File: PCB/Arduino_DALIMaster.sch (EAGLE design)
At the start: 13 parts, among them J1 22-27-2021-02, U1 ARDUINOR3-BPLACE

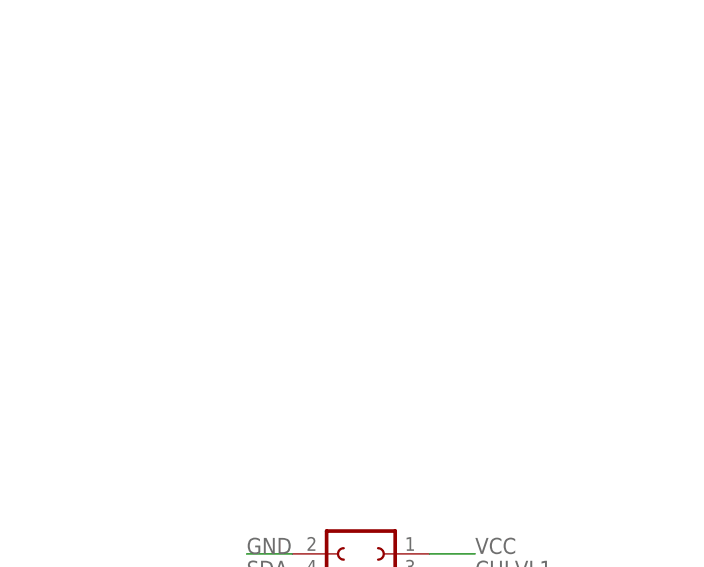
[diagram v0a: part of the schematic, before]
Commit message: SMT parts and rerouting
replaced all wired passives with 0603 SMT packages, rewired some of the
connections, reduced board size to 80x90mm
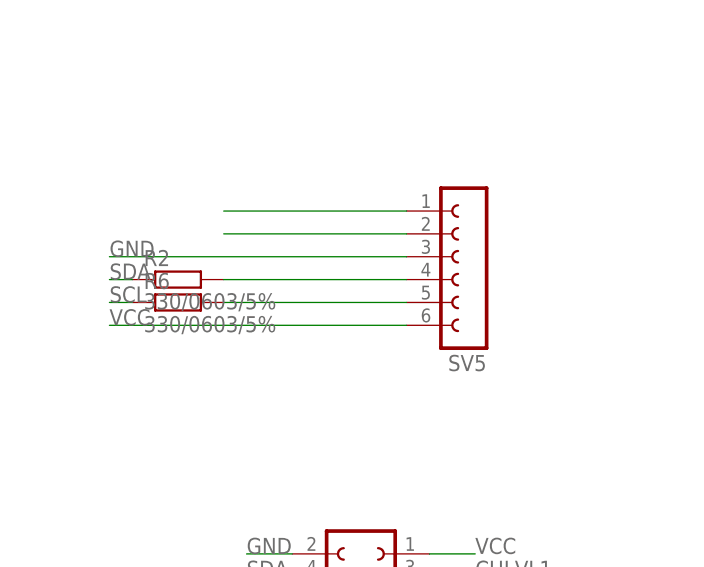
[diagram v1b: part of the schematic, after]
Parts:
- added R2, R6: 330/0603/5%, rcl:R-EU_R0603
- added SV5: (no value), con-lsta:FE06-1
- 2K7, R1, R3, R4, R5: device rcl:R-EU_0207/10 -> rcl:R-EU_R0603
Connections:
- new net N$2: SV5.1
- new net N$3: SV5.2
- new net N$5: R2.2, SV5.4
- new net N$6: R6.2, SV5.5
- net GND: now also SV5.3
- net SCL: now also R6.1
- net SDA: now also R2.1
- net VCC: now also SV5.6
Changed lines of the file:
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@@
 <grid distance="0.1" unitdist="inch" unit="inch" style="lines" multiple="1" display="no" altdistance="0.01" altunitdist="inch" altunit="inch"/>
 <layers>
-<layer number="1" name="Top" color="4" fill="1" visible="no" active="no"/>
-<layer number="16" name="Bottom" color="1" fill="1" visible="no" active="no"/>
-<layer number="17" name="Pads" color="2" fill="1" visible="no" active="no"/>
-<layer number="18" name="Vias" color="2" fill="1" visible="no" active="no"/>
-<layer number="19" name="Unrouted" color="6" fill="1" visible="no" active="no"/>
-<layer number="20" name="Dimension" color="15" fill="1" visible="no" active="no"/>
-<layer number="21" name="tPlace" color="14" fill="1" visible="no" active="no"/>
-<layer number="22" name="bPlace" color="7" fill="1" visible="no" active="no"/>
-<layer number="23" name="tOrigins" color="15" fill="1" visible="no" active="no"/>
-<layer number="24" name="bOrigins" color="15" fill="1" visible="no" active="no"/>
-<layer number="25" name="tNames" color="7" fill="1" visible="no" active="no"/>
-<layer number="26" name="bNames" color="7" fill="1" visible="no" active="no"/>
-<layer number="27" name="tValues" color="7" fill="1" visible="no" active="no"/>
-<layer number="28" name="bValues" color="7" fill="1" visible="no" active="no"/>
+<layer number="1" name="Top" color="4" fill="1" visible="yes" active="no"/>
+<layer number="16" name="Bottom" color="1" fill="1" visible="yes" active="no"/>
+<layer number="17" name="Pads" color="2" fill="1" visible="yes" active="no"/>
+<layer number="18" name="Vias" color="2" fill="1" visible="yes" active="no"/>
+<layer number="19" name="Unrouted" color="6" fill="1" visible="yes" active="no"/>
+<layer number="20" name="Dimension" color="15" fill="1" visible="yes" active="no"/>
+<layer number="21" name="tPlace" color="7" fill="1" visible="yes" active="no"/>
+<layer number="22" name="bPlace" color="7" fill="1" visible="yes" active="no"/>
+<layer number="23" name="tOrigins" color="15" fill="1" visible="yes" active="no"/>
+<layer number="24" name="bOrigins" color="15" fill="1" visible="yes" active="no"/>
+<layer number="25" name="tNames" color="7" fill="1" visible="yes" active="no"/>
+<layer number="26" name="bNames" color="7" fill="1" visible="yes" active="no"/>
+<layer number="27" name="tValues" color="7" fill="1" visible="yes" active="no"/>
+<layer number="28" name="bValues" color="7" fill="1" visible="yes" active="no"/>
 <layer number="29" name="tStop" color="7" fill="3" visible="no" active="no"/>
 <layer number="30" name="bStop" color="7" fill="6" visible="no" active="no"/>
@@
 <layer number="35" name="tGlue" color="7" fill="4" visible="no" active="no"/>
 <layer number="36" name="bGlue" color="7" fill="5" visible="no" active="no"/>
-<layer number="37" name="tTest" color="7" fill="1" visible="no" active="no"/>
-<layer number="38" name="bTest" color="7" fill="1" visible="no" active="no"/>
+<layer number="37" name="tTest" color="7" fill="1" visible="yes" active="no"/>
+<layer number="38" name="bTest" color="7" fill="1" visible="yes" active="no"/>
 <layer number="39" name="tKeepout" color="4" fill="11" visible="no" active="no"/>
 <layer number="40" name="bKeepout" color="1" fill="11" visible="no" active="no"/>
@@
 <layer number="44" name="Drills" color="7" fill="1" visible="no" active="no"/>
 <layer number="45" name="Holes" color="7" fill="1" visible="no" active="no"/>
-<layer number="46" name="Milling" color="3" fill="1" visible="no" active="no"/>
-<layer number="47" name="Measures" color="7" fill="1" visible="no" active="no"/>
-<layer number="48" name="Document" color="7" fill="1" visible="no" active="no"/>
-<layer number="49" name="Reference" color="7" fill="1" visible="no" active="no"/>
-<layer number="50" name="dxf" color="7" fill="1" visible="no" active="no"/>
-<layer number="51" name="tDocu" color="7" fill="1" visible="no" active="no"/>
-<layer number="52" name="bDocu" color="7" fill="1" visible="no" active="no"/>
-<layer number="53" name="tGND_GNDA" color="7" fill="9" visible="no" active="no"/>
-<layer number="54" name="bGND_GNDA" color="1" fill="9" visible="no" active="no"/>
-<layer number="56" name="wert" color="7" fill="1" visible="no" active="no"/>
-<layer number="57" name="tCAD" color="7" fill="1" visible="no" active="no"/>
+<layer number="46" name="Milling" color="3" fill="1" visible="yes" active="no"/>
+<layer number="47" name="Measures" color="7" fill="1" visible="yes" active="no"/>
+<layer number="48" name="Document" color="7" fill="1" visible="yes" active="no"/>
+<layer number="49" name="Reference" color="7" fill="1" visible="yes" active="no"/>
+<layer number="50" name="dxf" color="7" fill="1" visible="yes" active="no"/>
+<layer number="51" name="tDocu" color="7" fill="1" visible="yes" active="no"/>
+<layer number="52" name="bDocu" color="7" fill="1" visible="yes" active="no"/>
+<layer number="53" name="tGND_GNDA" color="7" fill="9" visible="yes" active="no"/>
+<layer number="54" name="bGND_GNDA" color="1" fill="9" visible="yes" active="no"/>
+<layer number="56" name="wert" color="7" fill="1" visible="yes" active="no"/>
+<layer number="57" name="tCAD" color="7" fill="1" visible="yes" active="no"/>
 <layer number="90" name="Modules" color="5" fill="1" visible="yes" active="yes"/>
 <layer number="91" name="Nets" color="2" fill="1" visible="yes" active="yes"/>
@@
 <part name="SV3" library="con-lsta" deviceset="FE05-2" device=""/>
 <part name="SV4" library="con-lsta" deviceset="FE05-2" device=""/>
-<part name="R1" library="rcl" deviceset="R-EU_" device="0207/10" value="2k7"/>
-<part name="2K7" library="rcl" deviceset="R-EU_" device="0207/10"/>
-<part name="R3" library="rcl" deviceset="R-EU_" device="0207/10"/>
-<part name="R4" library="rcl" deviceset="R-EU_" device="0207/10"/>
-<part name="R5" library="rcl" deviceset="R-EU_" device="0207/10"/>
+<part name="R1" library="rcl" deviceset="R-EU_" device="R0603" value="2k7"/>
+<part name="2K7" library="rcl" deviceset="R-EU_" device="R0603"/>
+<part name="R3" library="rcl" deviceset="R-EU_" device="R0603"/>
+<part name="R4" library="rcl" deviceset="R-EU_" device="R0603"/>
+<part name="R5" library="rcl" deviceset="R-EU_" device="R0603"/>
 <part name="GND1" library="supply1" deviceset="GND" device=""/>
 <part name="J1" library="con-molex" deviceset="22-?-02" device="27-2021"/>
@@
 <part name="U$1" library="codemercs" deviceset="WARRIOR11" device=""/>
 <part name="U$2" library="codemercs" deviceset="WARRIOR09MOD1" device=""/>
+<part name="SV5" library="con-lsta" deviceset="FE06-1" device=""/>
+<part name="R2" library="rcl" deviceset="R-EU_" device="R0603" value="330/0603/5%"/>
+<part name="R6" library="rcl" deviceset="R-EU_" device="R0603" value="330/0603/5%"/>
 </parts>
 <sheets>
@@
 <instance part="U$1" gate="G$1" x="147.32" y="38.1"/>
 <instance part="U$2" gate="G$1" x="119.38" y="63.5"/>
+<instance part="SV5" gate="G$1" x="91.44" y="152.4" rot="R180"/>
+<instance part="R2" gate="G$1" x="58.42" y="149.86"/>
+<instance part="R6" gate="G$1" x="58.42" y="147.32"/>
 </instances>
 <busses>
@@
 <pinref part="GND2" gate="1" pin="GND"/>
 </segment>
+<segment>
+<pinref part="SV5" gate="G$1" pin="3"/>
+<wire x1="83.82" y1="152.4" x2="50.8" y2="152.4" width="0.1524" layer="91"/>
+<label x="50.8" y="152.4" size="1.778" layer="95"/>
+</segment>
 </net>
 <net name="SDA" class="0">
@@
 <wire x1="109.22" y1="236.22" x2="124.46" y2="236.22" width="0.1524" layer="91"/>
 </segment>
+<segment>
+<pinref part="R2" gate="G$1" pin="1"/>
+<wire x1="53.34" y1="149.86" x2="50.8" y2="149.86" width="0.1524" layer="91"/>
+<label x="50.8" y="149.86" size="1.778" layer="95"/>
+</segment>
 </net>
 <net name="SCL" class="0">
@@
 <wire x1="116.84" y1="238.76" x2="109.22" y2="238.76" width="0.1524" layer="91"/>
 <pinref part="U1" gate="G$1" pin="SCL"/>
+</segment>
+<segment>
+<pinref part="R6" gate="G$1" pin="1"/>
+<wire x1="53.34" y1="147.32" x2="50.8" y2="147.32" width="0.1524" layer="91"/>
+<label x="50.8" y="147.32" size="1.778" layer="95"/>
 </segment>
 </net>
@@
 <wire x1="121.92" y1="210.82" x2="121.92" y2="215.9" width="0.1524" layer="91"/>
 <label x="121.92" y="215.9" size="1.778" layer="95"/>
+</segment>
+<segment>
+<pinref part="SV5" gate="G$1" pin="6"/>
+<wire x1="83.82" y1="144.78" x2="50.8" y2="144.78" width="0.1524" layer="91"/>
+<label x="50.8" y="144.78" size="1.778" layer="95"/>
 </segment>
 </net>
@@
 </segment>
 </net>
+<net name="N$2" class="0">
+<segment>
+<pinref part="SV5" gate="G$1" pin="1"/>
+<wire x1="83.82" y1="157.48" x2="63.5" y2="157.48" width="0.1524" layer="91"/>
+</segment>
+</net>
+<net name="N$3" class="0">
+<segment>
+<pinref part="SV5" gate="G$1" pin="2"/>
+<wire x1="83.82" y1="154.94" x2="63.5" y2="154.94" width="0.1524" layer="91"/>
+</segment>
+</net>
+<net name="N$5" class="0">
+<segment>
+<pinref part="SV5" gate="G$1" pin="4"/>
+<wire x1="83.82" y1="149.86" x2="63.5" y2="149.86" width="0.1524" layer="91"/>
+<pinref part="R2" gate="G$1" pin="2"/>
+</segment>
+</net>
+<net name="N$6" class="0">
+<segment>
+<pinref part="SV5" gate="G$1" pin="5"/>
+<wire x1="83.82" y1="147.32" x2="63.5" y2="147.32" width="0.1524" layer="91"/>
+<pinref part="R6" gate="G$1" pin="2"/>
+</segment>
+</net>
